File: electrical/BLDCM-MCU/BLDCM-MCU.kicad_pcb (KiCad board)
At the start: 4 copper layers, 32 x 32 mm, 85 parts, among them J1 52991-0308, K1 EVPAKE31A, U1 STM32F446RE, U10 SK6805, U11 SK6805, U12 SK6805, U13 SK6805, U14 SK6805, U15 SK6805, U16 SK6805, U17 SK6805, U18 SK6805, U19 SK6805, U2 SN74LV1T34DBVR, U20 MT6701, U3 ISM330DHCX, U4 SK6805, U5 SK6805, U6 SK6805, U7 SK6805, U8 SK6805, U9 SK6805, Y1 ECS-3225MVLC-240-CN

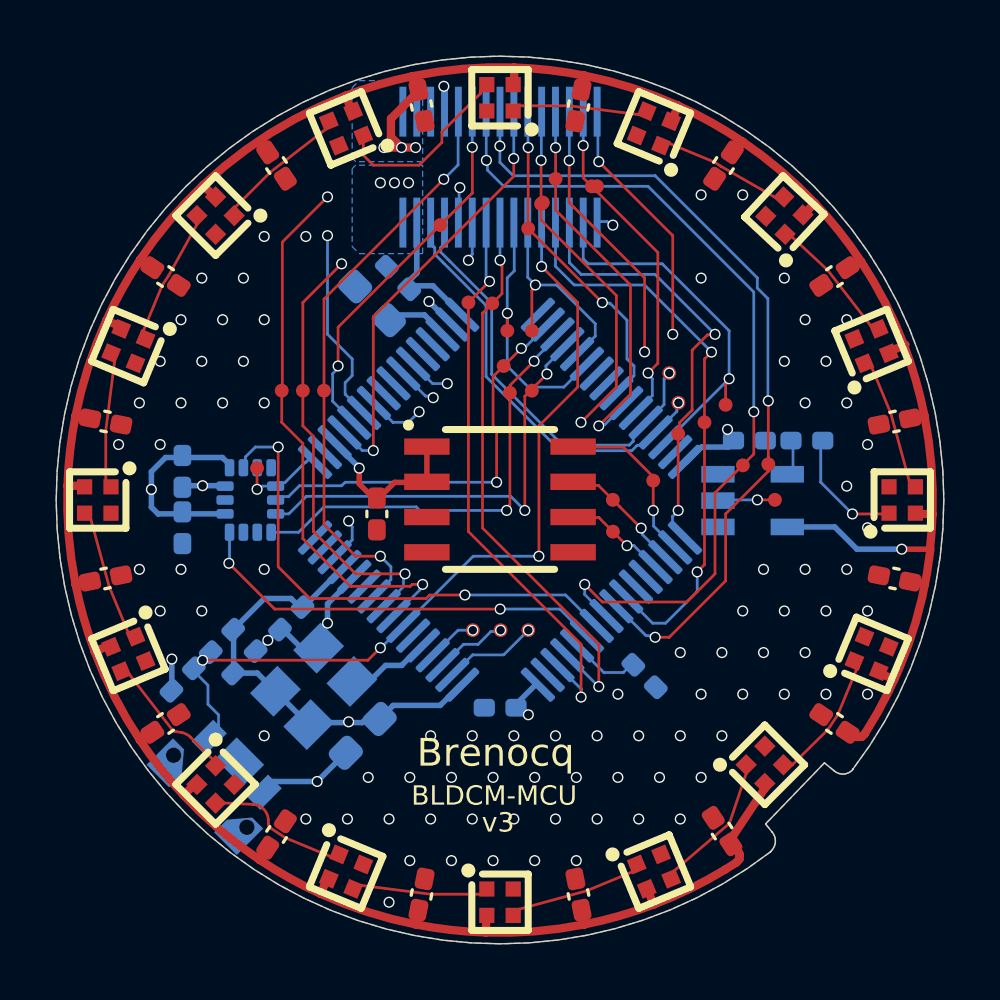
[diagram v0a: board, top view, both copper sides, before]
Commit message: Fix: PCB resistor rotation
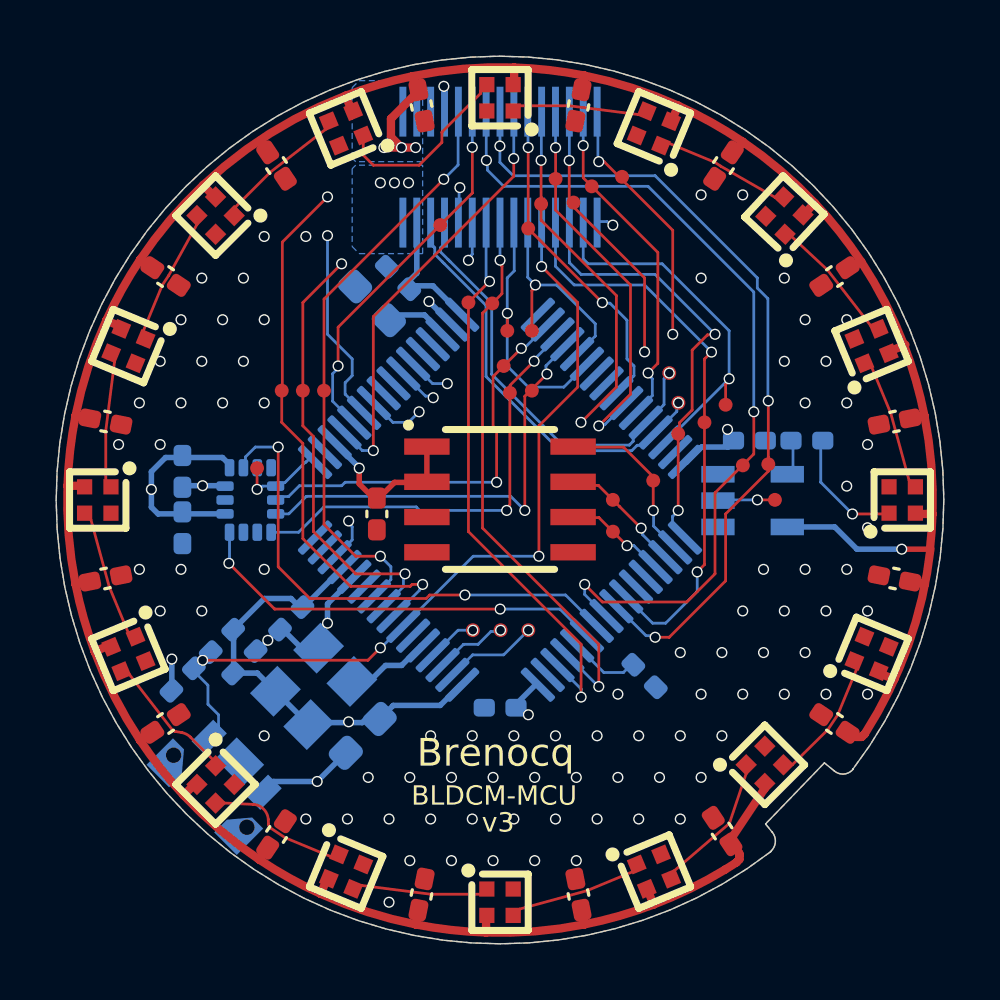
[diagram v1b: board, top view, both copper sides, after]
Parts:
- moved TP2 1.11 mm to (151.2, 94.3)
- moved TP4 0.96 mm to (152.9, 93.4)
- turned C10 to 90 degrees
- turned C11 to 11.25 degrees
- turned C12 to 33.75 degrees
- turned C13 to 56.25 degrees
- turned C14 to 78.75 degrees
- turned C15 to 101.25 degrees
- turned C16 to 123.75 degrees
- turned C17 to 146.25 degrees
- turned C18 to 168.75 degrees
- turned C19 to -168.75 degrees
- turned C2 to 45 degrees
- turned C20 to -146.25 degrees
- turned C21 to -123.75 degrees
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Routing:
- net RST: track 30.4 -> 0.00 mm, vias 4 -> 0
- net (no net): track 0.00 -> 30.4 mm, vias 0 -> 4
- net TMC.UL: track 20.9 -> 0.00 mm, vias 3 -> 0
- net /TMC.UL: track 0.00 -> 20.9 mm, vias 0 -> 3
- net TMC.WH: track 12.4 -> 0.00 mm, vias 2 -> 0
- net /TMC.WH: track 0.00 -> 12.4 mm, vias 0 -> 2
- net NetR5_2: track 4.44 -> 0.00 mm, vias 1 -> 0
- net Net-(U4-DI): track 0.00 -> 4.44 mm, vias 0 -> 1
- net BOOT0: track 2.57 -> 0.00 mm
- net /BOOT0: track 0.00 -> 2.57 mm
- net NetR5_1: track 1.31 -> 0.00 mm
- net Net-(U2-OUT): track 0.00 -> 1.31 mm
